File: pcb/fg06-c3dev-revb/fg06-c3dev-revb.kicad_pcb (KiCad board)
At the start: 2 copper layers, 90 x 55 mm, 17 parts, among them J1 Conn_01x12, SW1 SW_Push, U1 AE-USB2.0-TYPE-C, U2 M5STAMP-C3, U3 KMR-1.8SPI

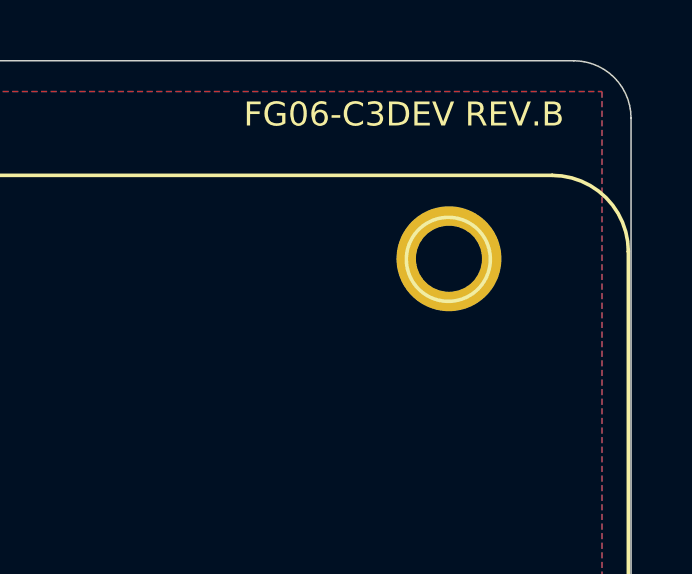
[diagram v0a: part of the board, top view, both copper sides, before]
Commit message: gerber data update (There are no modifications to the circuit. More accurate correction of screw hole position)
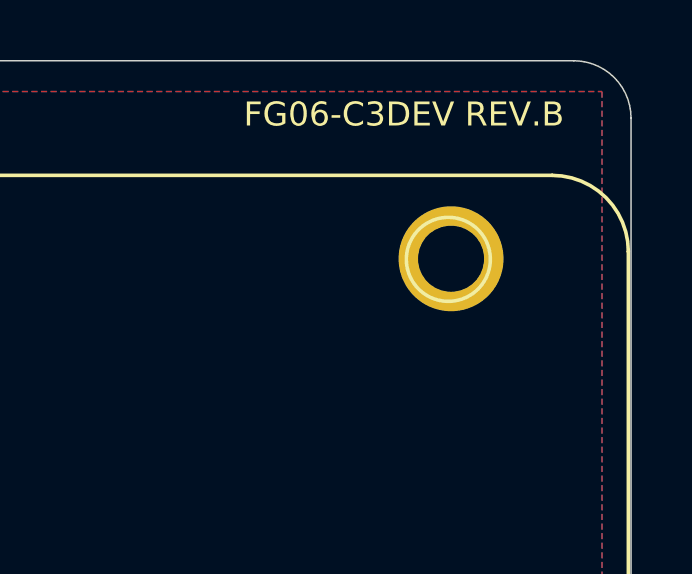
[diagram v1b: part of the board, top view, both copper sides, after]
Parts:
- moved REF3 0.07 mm to (124.0, 44.7)
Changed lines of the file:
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@@
   )
   (footprint "MountingHole:MountingHole_2.2mm_M2_ISO7380_Pad" locked (layer "F.Cu")
-    (at 123.93 44.69)
+    (at 124 44.69)
     (descr "Mounting Hole 2.2mm, M2, ISO7380")
     (tags "mounting hole 2.2mm m2 iso7380")
